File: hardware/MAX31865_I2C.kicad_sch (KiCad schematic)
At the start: 21 parts, among them J1 Conn_01x08, J2 AVR-ISP-6, J3 Conn_02x04_Odd_Even, U1 ATmega48A-A, Y1 16MHz

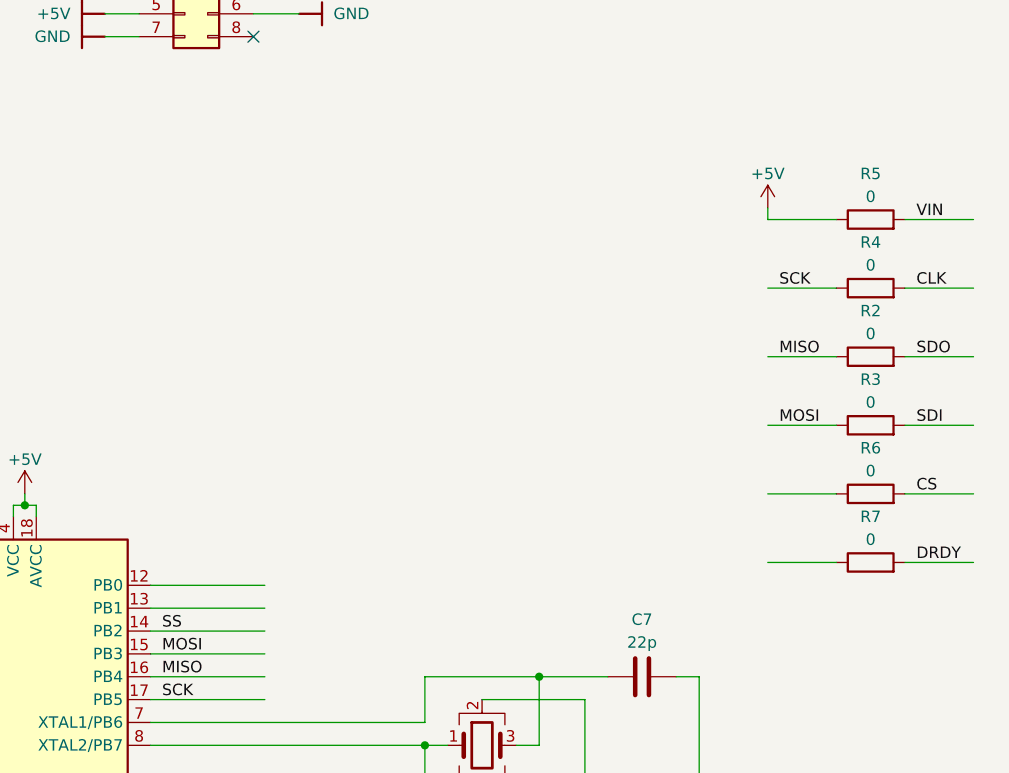
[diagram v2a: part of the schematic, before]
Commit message: connected CS and DRDY of MAX31865 module
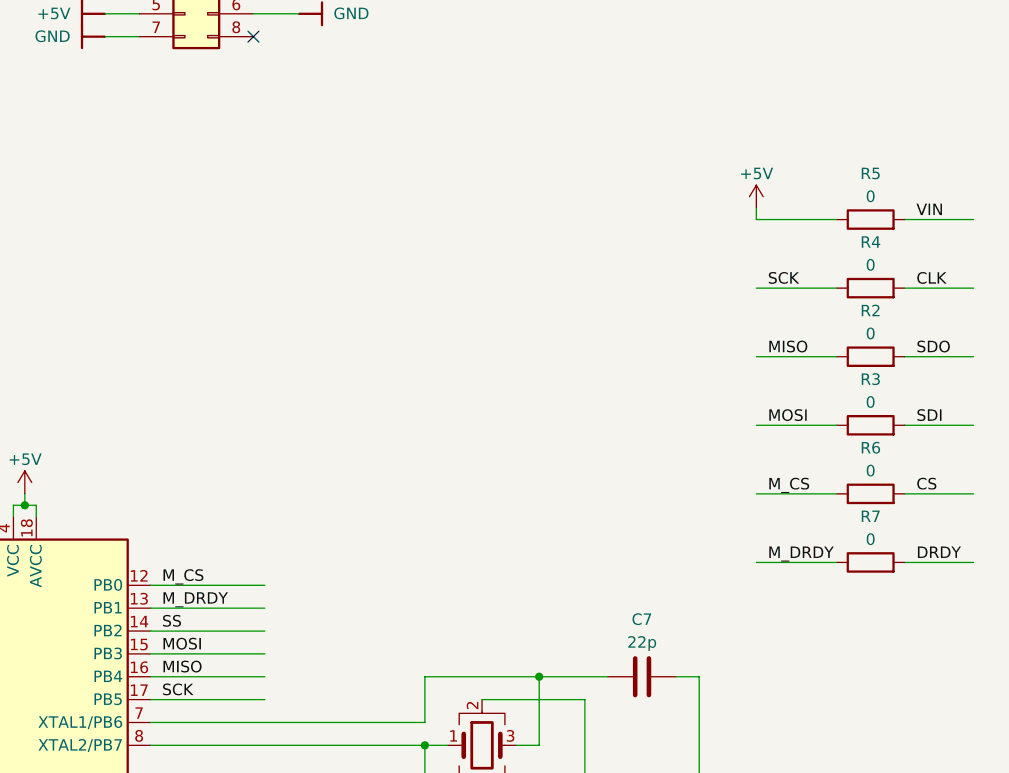
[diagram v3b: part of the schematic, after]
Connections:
- net M_CS: now reaches U1.12 (PB0)
- net M_CS: now also R6.1
- net M_DRDY: now reaches U1.13 (PB1)
- net M_DRDY: now also R7.1
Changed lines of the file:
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@@
-    (stroke (width 0) (type default))
-  )
-  (wire (pts (xy 187.96 30.48) (xy 195.58 30.48))
     (stroke (width 0) (type default))
   )
@@
     (stroke (width 0) (type default))
   )
+  (wire (pts (xy 186.69 53.34) (xy 195.58 53.34))
+    (stroke (width 0) (type default))
+  )
   (wire (pts (xy 231.14 43.18) (xy 241.3 43.18))
     (stroke (width 0) (type default))
@@
     (stroke (width 0) (type default))
   )
-  (wire (pts (xy 187.96 15.24) (xy 195.58 15.24))
+  (wire (pts (xy 186.69 15.24) (xy 195.58 15.24))
     (stroke (width 0) (type default))
   )
@@
     (stroke (width 0) (type default))
   )
-  (wire (pts (xy 187.96 22.86) (xy 195.58 22.86))
+  (wire (pts (xy 186.69 38.1) (xy 195.58 38.1))
+    (stroke (width 0) (type default))
+  )
+  (wire (pts (xy 186.69 22.86) (xy 195.58 22.86))
     (stroke (width 0) (type default))
   )
@@
     (stroke (width 0) (type default))
   )
-  (wire (pts (xy 187.96 13.97) (xy 187.96 15.24))
-    (stroke (width 0) (type default))
-  )
-  (wire (pts (xy 187.96 45.72) (xy 195.58 45.72))
+  (wire (pts (xy 186.69 13.97) (xy 186.69 15.24))
+    (stroke (width 0) (type default))
+  )
+  (wire (pts (xy 186.69 45.72) (xy 195.58 45.72))
     (stroke (width 0) (type default))
   )
@@
   )
   (wire (pts (xy 119.38 101.6) (xy 132.08 101.6))
-    (stroke (width 0) (type default))
-  )
-  (wire (pts (xy 187.96 53.34) (xy 195.58 53.34))
     (stroke (width 0) (type default))
   )
@@
     (stroke (width 0) (type default))
   )
-  (wire (pts (xy 187.96 38.1) (xy 195.58 38.1))
+  (wire (pts (xy 186.69 30.48) (xy 195.58 30.48))
     (stroke (width 0) (type default))
   )
@@
     (effects (font (size 1.27 1.27)) (justify left bottom))
   )
-  (label "SCK" (at 189.23 22.86 0) (fields_autoplaced)
+  (label "M_CS" (at 120.65 55.88 0) (fields_autoplaced)
+    (effects (font (size 1.27 1.27)) (justify left bottom))
+  )
+  (label "SCK" (at 187.96 22.86 0) (fields_autoplaced)
     (effects (font (size 1.27 1.27)) (justify left bottom))
   )
@@
     (effects (font (size 1.27 1.27)) (justify left bottom))
   )
+  (label "M_DRDY" (at 187.96 53.34 0) (fields_autoplaced)
+    (effects (font (size 1.27 1.27)) (justify left bottom))
+  )
   (label "CLK" (at 234.95 33.02 0) (fields_autoplaced)
     (effects (font (size 1.27 1.27)) (justify left bottom))
@@
     (effects (font (size 1.27 1.27)) (justify left bottom))
   )
-  (label "MOSI" (at 189.23 38.1 0) (fields_autoplaced)
+  (label "MOSI" (at 187.96 38.1 0) (fields_autoplaced)
     (effects (font (size 1.27 1.27)) (justify left bottom))
   )
@@
     (effects (font (size 1.27 1.27)) (justify left bottom))
   )
-  (label "MISO" (at 189.23 30.48 0) (fields_autoplaced)
+  (label "MISO" (at 187.96 30.48 0) (fields_autoplaced)
+    (effects (font (size 1.27 1.27)) (justify left bottom))
+  )
+  (label "M_CS" (at 187.96 45.72 0) (fields_autoplaced)
     (effects (font (size 1.27 1.27)) (justify left bottom))
   )
   (label "SCK" (at 120.65 68.58 0) (fields_autoplaced)
+    (effects (font (size 1.27 1.27)) (justify left bottom))
+  )
+  (label "M_DRDY" (at 120.65 58.42 0) (fields_autoplaced)
     (effects (font (size 1.27 1.27)) (justify left bottom))
   )
@@
     )
   )
-  (symbol (lib_id "power:+5V") (at 187.96 13.97 0) (unit 1)
-    (in_bom yes) (on_board yes) (dnp no) (fields_autoplaced)
-    (property "Reference" "#PWR021" (at 187.96 17.78 0)
-      (effects (font (size 1.27 1.27)) hide)
-    )
-    (property "Value" "+5V" (at 187.96 10.16 0)
-      (effects (font (size 1.27 1.27)))
-    )
-    (property "Footprint" "" (at 187.96 13.97 0)
-      (effects (font (size 1.27 1.27)) hide)
-    )
-    (property "Datasheet" "" (at 187.96 13.97 0)
-      (effects (font (size 1.27 1.27)) hide)
-    )
+  (symbol (lib_id "power:+5V") (at 186.69 13.97 0) (unit 1)
+    (in_bom yes) (on_board yes) (dnp no) (fields_autoplaced)
+    (property "Reference" "#PWR021" (at 186.69 17.78 0)
+      (effects (font (size 1.27 1.27)) hide)
+    )
+    (property "Value" "+5V" (at 186.69 10.16 0)
+      (effects (font (size 1.27 1.27)))
+    )
+    (property "Footprint" "" (at 186.69 13.97 0)
+      (effects (font (size 1.27 1.27)) hide)
+    )
+    (property "Datasheet" "" (at 186.69 13.97 0)
+      (effects (font (size 1.27 1.27)) hide)
+    )

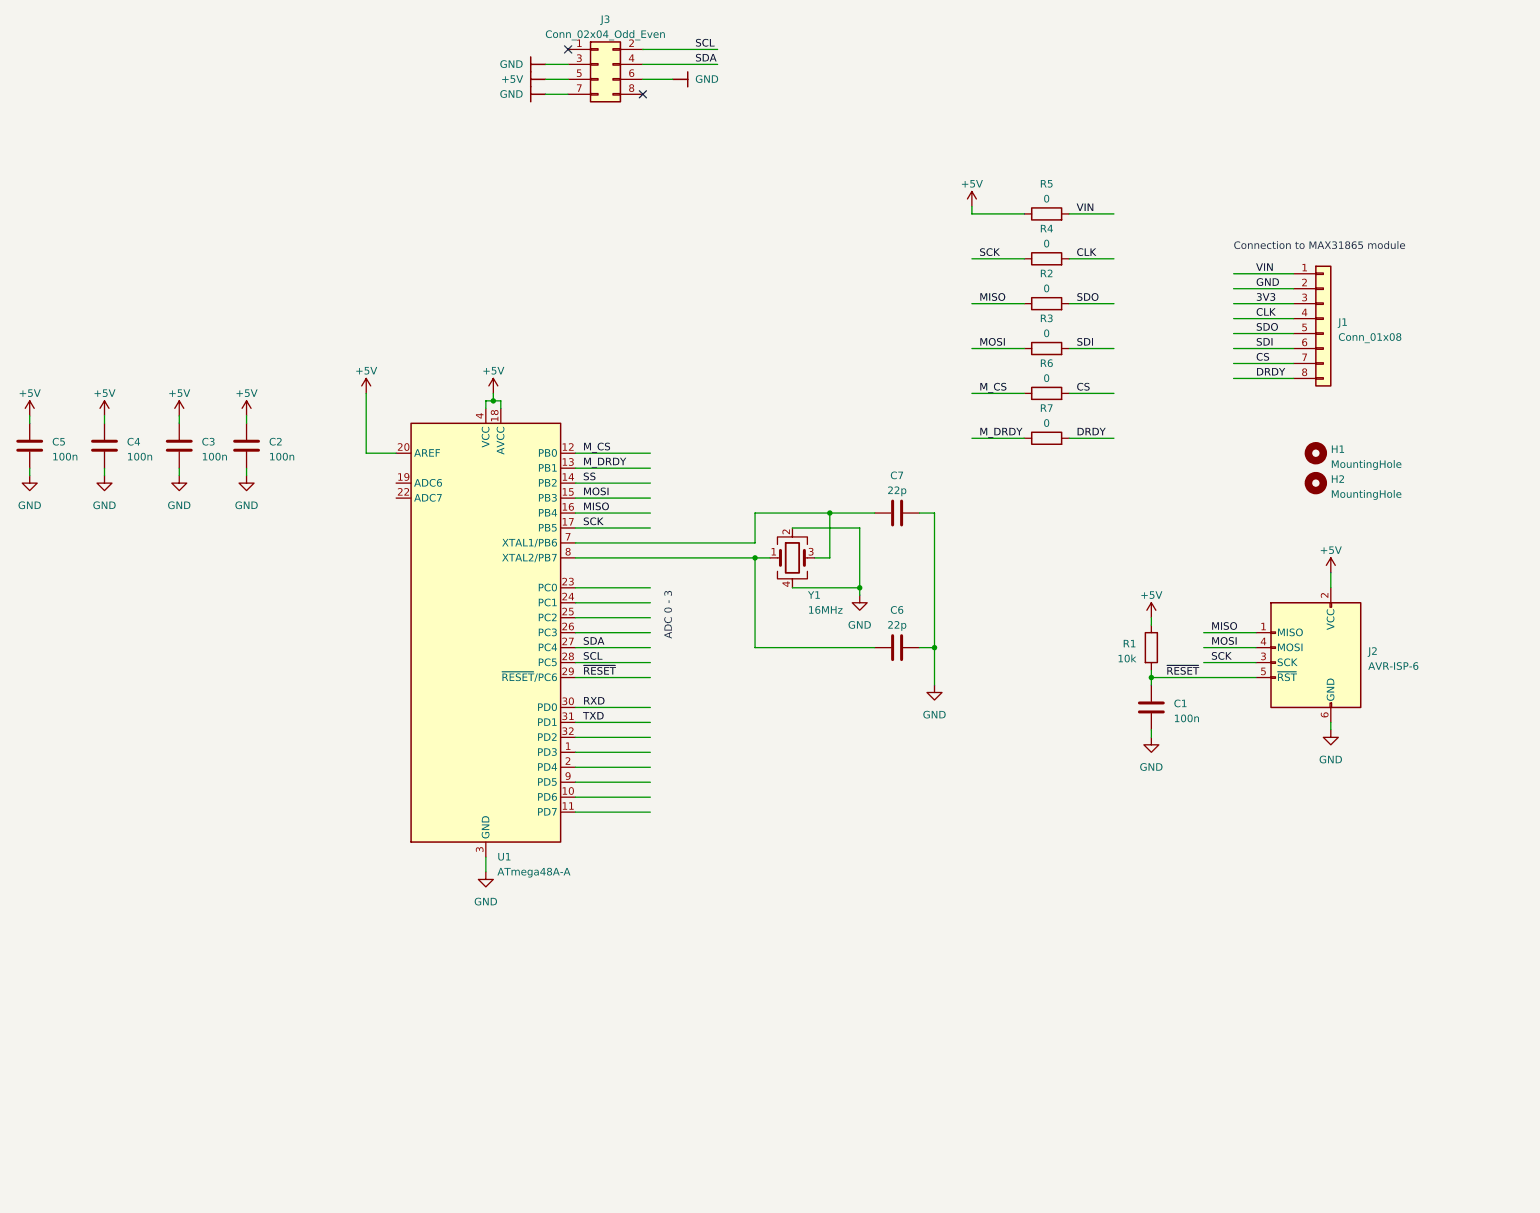
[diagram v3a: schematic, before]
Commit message: added template for schematic and cleaned PCB a tiny bit
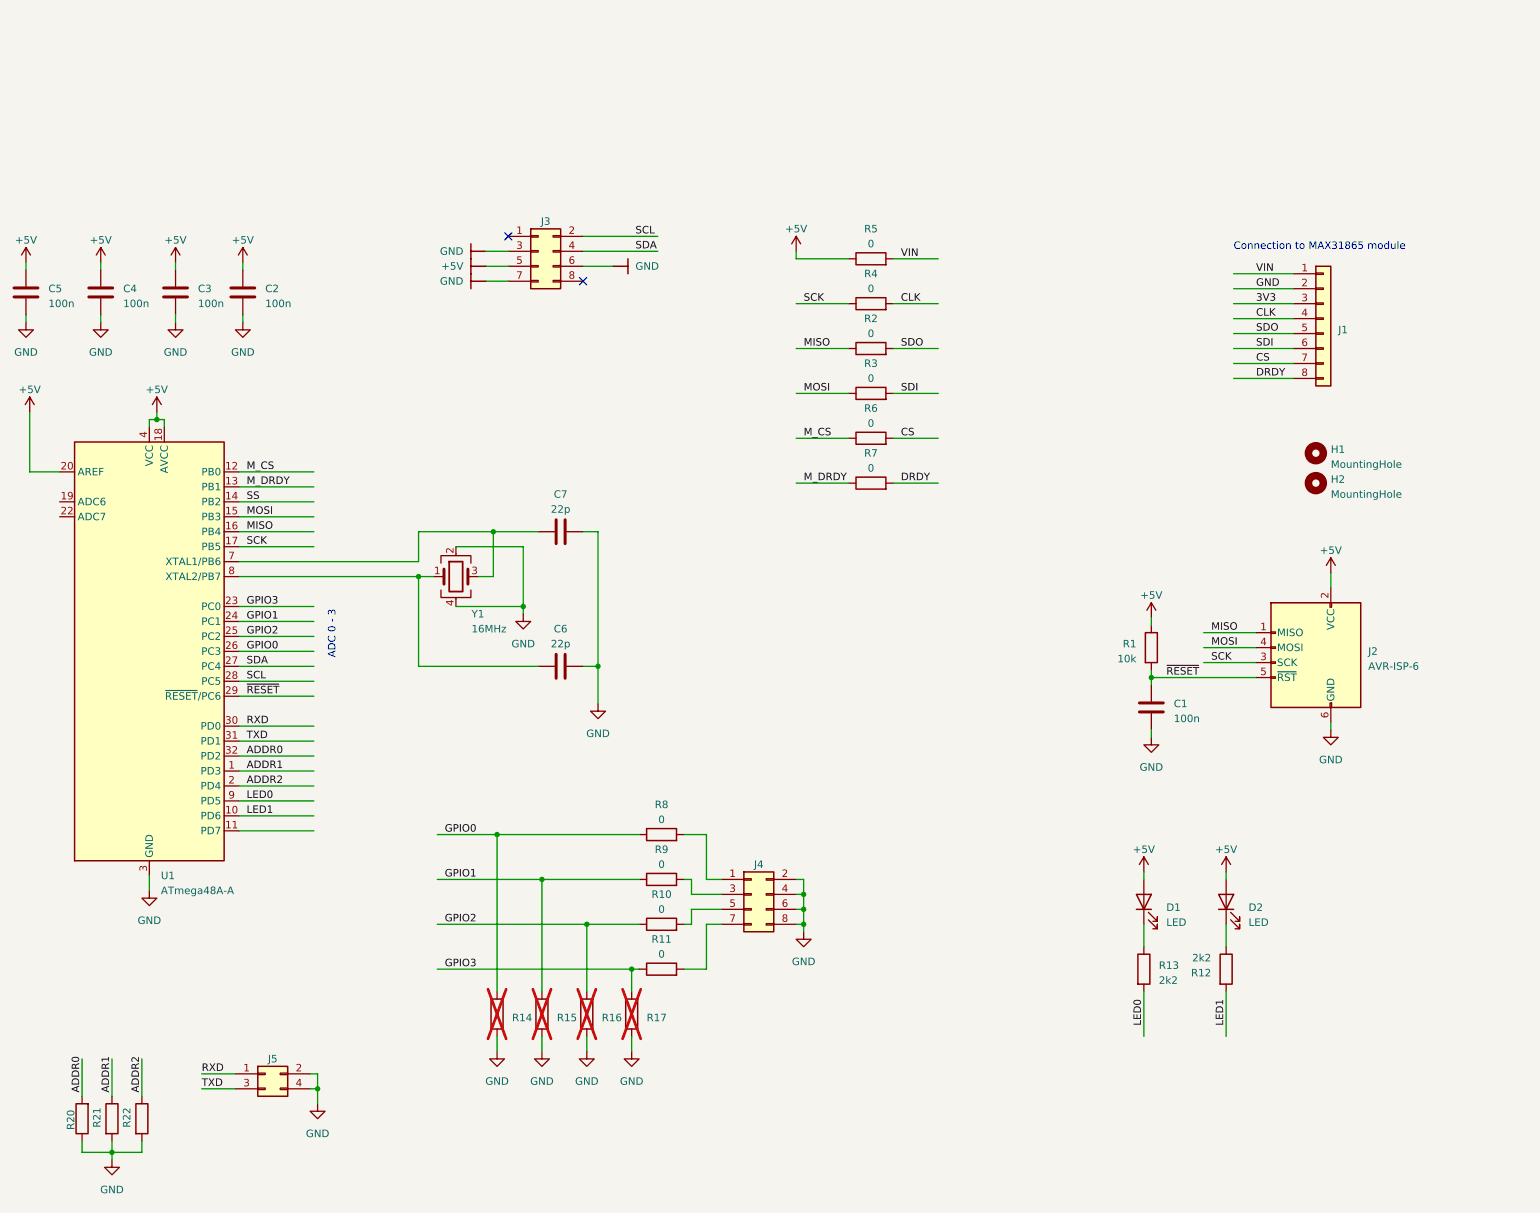
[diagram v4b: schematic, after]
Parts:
- added D1, D2: LED, LED_SMD:LED_0603_1608Metric, symbol Device:LED
- added J4: Conn_02x04_Odd_Even, PinHeaderEdgeMount:PinHeader_2x04_P2.54mm_Edge, symbol Connector_Generic:Conn_02x04_Odd_Even
- added J5: Conn_02x02_Odd_Even, PinHeaderEdgeMount:PinHeader_2x02_P2.54mm_Edge, symbol Connector_Generic:Conn_02x02_Odd_Even
- added R10, R11, R8, R9: 0, Resistor_SMD:R_0603_1608Metric, symbol Device:R
- added R12, R13: 2k2, Resistor_SMD:R_0603_1608Metric, symbol Device:R
- added R14, R15, R16, R17, R20, R21, R22: ~, Resistor_SMD:R_0603_1608Metric, symbol Device:R
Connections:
- net +5V: now also D1.2 (A), D2.2 (A)
- net GND: now also J4.2 (Pin_2), J4.4 (Pin_4), J4.6 (Pin_6), J4.8 (Pin_8), J5.2 (Pin_2), J5.4 (Pin_4), R14.1, R15.1, R16.1, R17.1, R20.1, R21.2, R22.2
- net RXD: now also J5.1 (Pin_1)
- net TXD: now also J5.3 (Pin_3)
- net ADDR1: now reaches U1.1 (PD3)
- net ADDR1: now also R21.1
- net LED1: now reaches U1.10 (PD6)
- net LED1: now also R12.2
- net ADDR2: now reaches U1.2 (PD4)
- net ADDR2: now also R22.1
- net GPIO3: now reaches U1.23 (PC0)
- net GPIO3: now also R11.1, R17.2
- net GPIO1: now reaches U1.24 (PC1)
- net GPIO1: now also R15.2, R9.1
- net GPIO2: now reaches U1.25 (PC2)
- net GPIO2: now also R10.1, R16.2
- net GPIO0: now reaches U1.26 (PC3)
- net GPIO0: now also R14.2, R8.1
- net ADDR0: now reaches U1.32 (PD2)
- net ADDR0: now also R20.2
- net LED0: now reaches U1.9 (PD5)
- net LED0: now also R13.2
- new net: D1.1 (K), R13.1
- new net: D2.1 (K), R12.1
- new net: J4.5 (Pin_5), R10.2
- new net: J4.1 (Pin_1), R8.2
- new net: J4.7 (Pin_7), R11.2
- new net: J4.3 (Pin_3), R9.2
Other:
- company: (none) -> Jochi St
- title: (none) -> MAX31865 I2C bridge
- moved on the sheet: C2, C3, C4, C5, C6, C7, J3, R2, R3, R4, R5, R6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

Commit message: ERC and DRC clean
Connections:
- no-connect marks 2 -> 6
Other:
- moved on the sheet: C2, C3, C4, C5, C6, C7, J4, J5, R10, R11, R14, R15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
